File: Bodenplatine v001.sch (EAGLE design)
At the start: 104 parts, among them K1 RY612012, K2 RY612012, K3 RY612012, K4 RY612012, K5 RY612012, K6 RY612012, K7 RY612012, K8 RY612012, K9 RY612012, Q1 BC846, Q2 BC846, Q3 BC846, Q4 BC846, Q5 BC846, Q6 BC846, Q7 BC846, Q8 BC846, Q9 BC846, X1 SPRINGCON_AST125_5X2, X10 SPRINGCON_AST125_3X2, X11 SPRINGCON_AST125_4X2, X12 SPRINGCON_AST125_4X2, X13 SPRINGCON_AST125_5X2, X14 236-403, X15 236-402, X2 SPRINGCON_AST125_5X2, X3 SPRINGCON_AST125_5X2, X4 SPRINGCON_AST125_5X2, X5 SPRINGCON_AST125_5X2, X6 SPRINGCON_AST125_5X2, X7 SPRINGCON_AST125_5X2, X8 SPRINGCON_AST125_5X2, X9 SPRINGCON_AST125_5X2

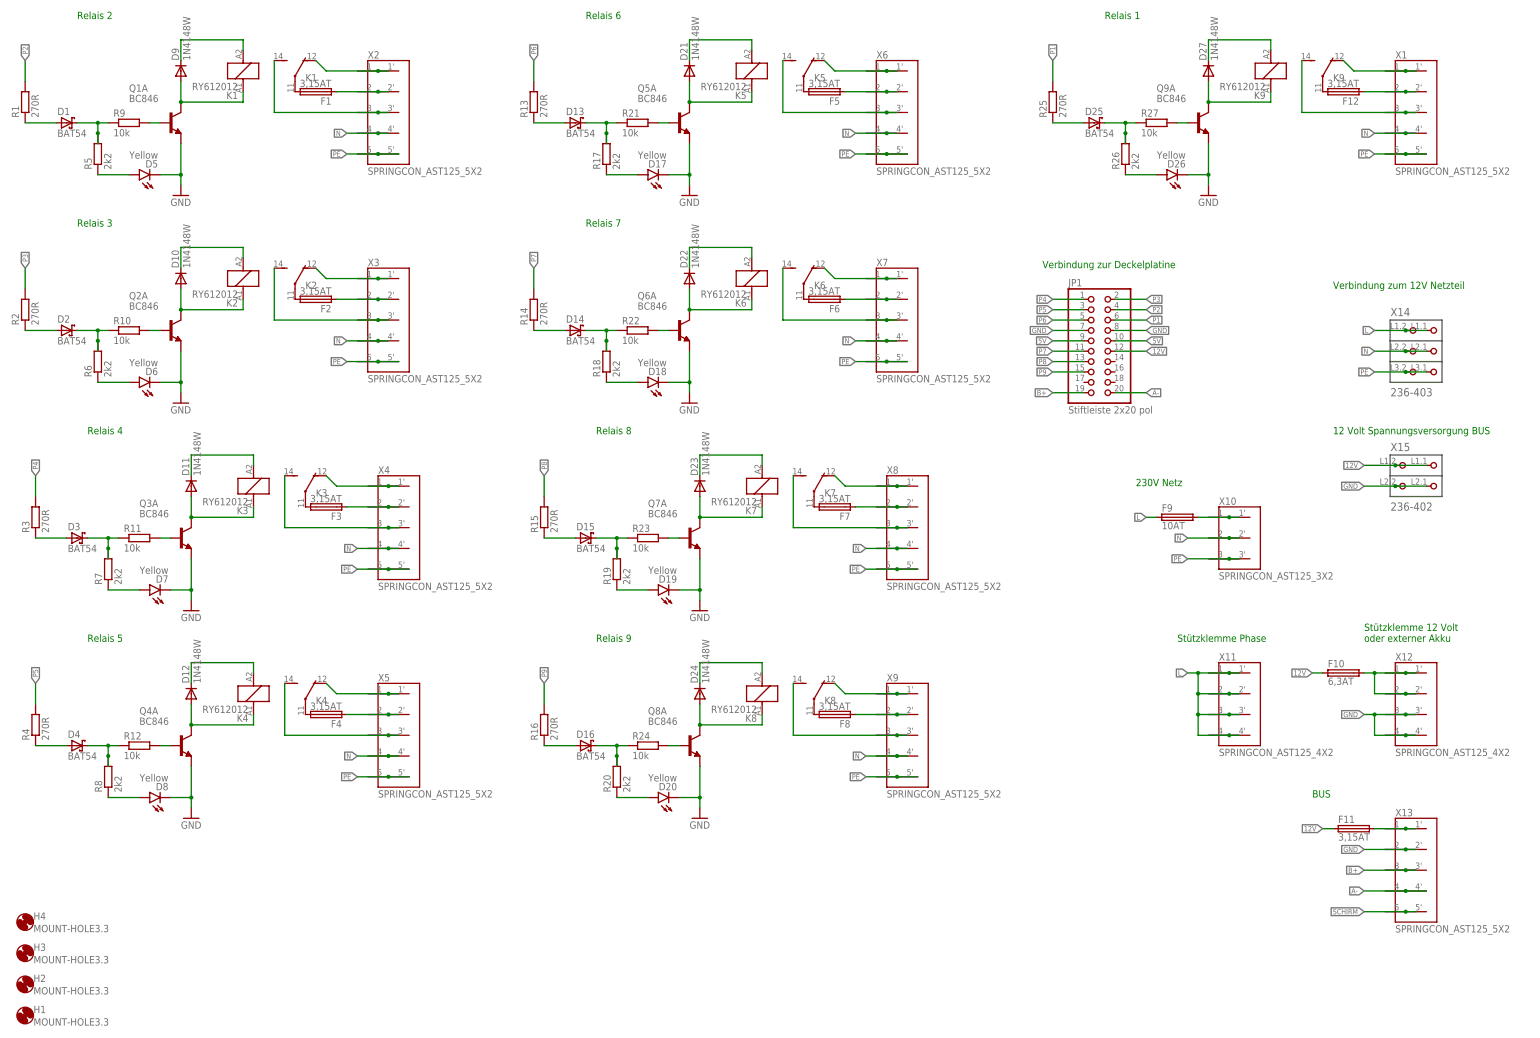
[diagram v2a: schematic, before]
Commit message: Relais neu sortiert (umbenannt)
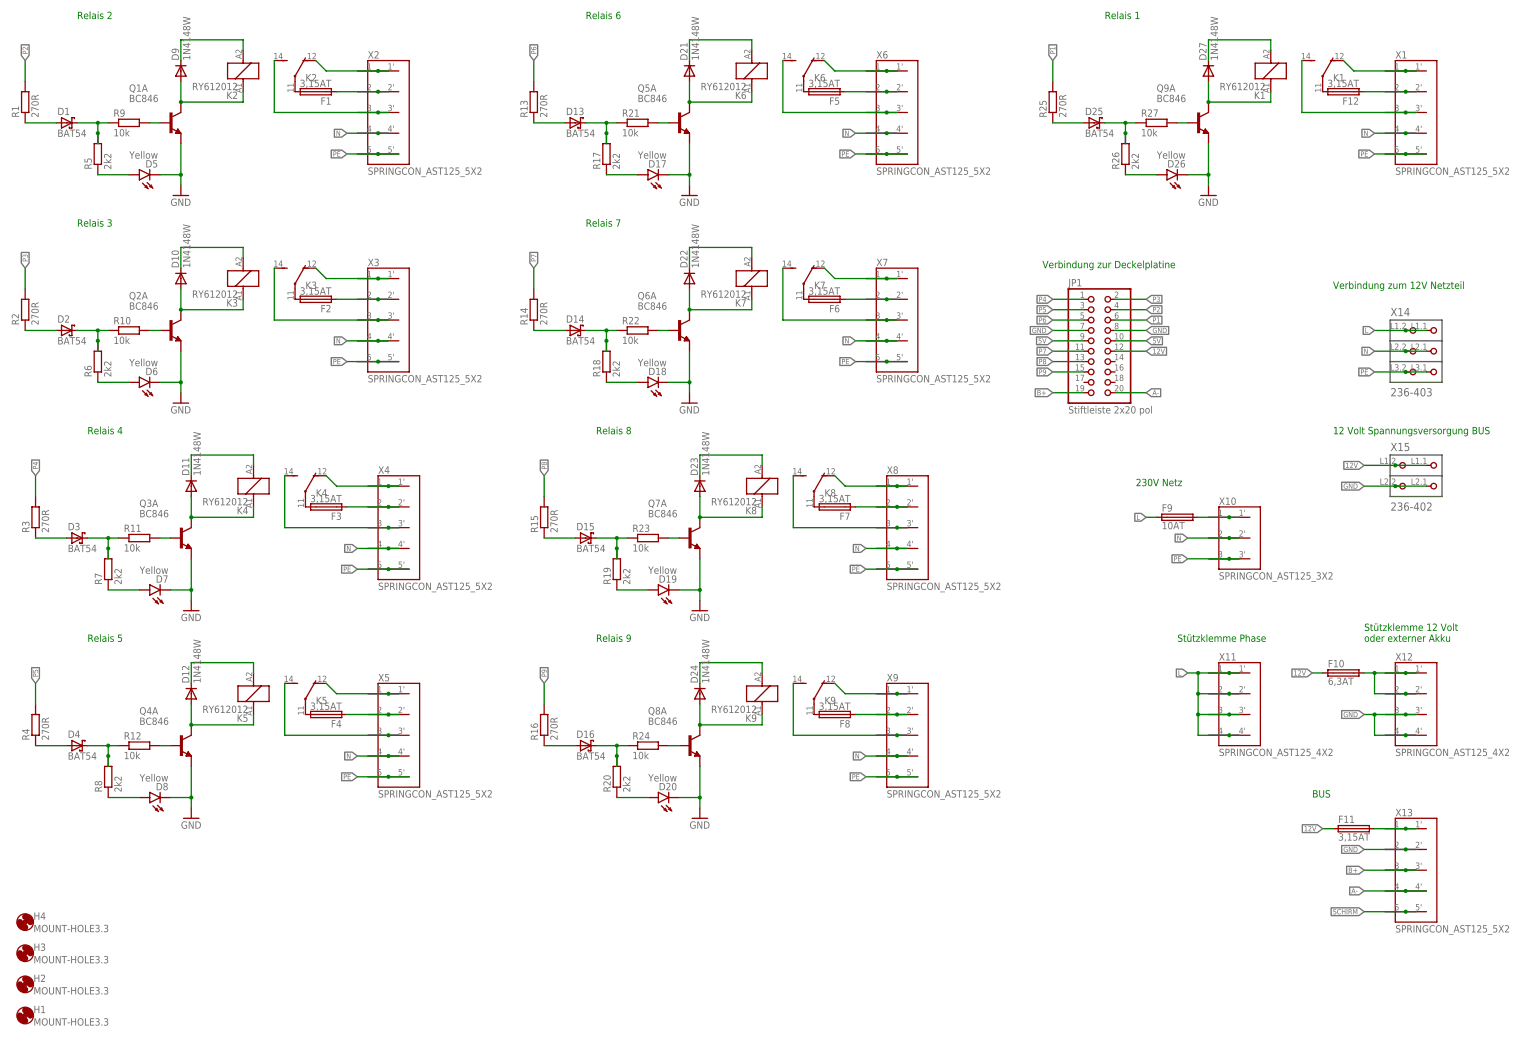
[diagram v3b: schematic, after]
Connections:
- net N$11: now also K21.2; no longer K11.2
- net N$12: now also K32.P; no longer K22.P
- net N$17: now also K31.2; no longer K21.2
- net N$18: now also K31.1; no longer K21.1
- net N$2: now also K22.S; no longer K12.S
- net N$20: now also K32.O; no longer K22.O
- net N$21: now also K42.S; no longer K32.S
- net N$22: now also K42.P; no longer K32.P
- net N$27: now also K41.2; no longer K31.2
- net N$28: now also K41.1; no longer K31.1
- net N$3: now also K22.P; no longer K12.P
- net N$30: now also K42.O; no longer K32.O
- net N$31: now also K52.S; no longer K42.S
- net N$32: now also K52.P; no longer K42.P
- net N$37: now also K51.2; no longer K41.2
- net N$38: now also K51.1; no longer K41.1
- net N$4: now also K22.O; no longer K12.O
- net N$40: now also K52.O; no longer K42.O
- net N$41: now also K62.S; no longer K52.S
- net N$42: now also K62.P; no longer K52.P
- net N$47: now also K61.2; no longer K51.2
- net N$48: now also K61.1; no longer K51.1
- net N$5: now also K21.1; no longer K11.1
- net N$50: now also K62.O; no longer K52.O
- net N$51: now also K72.S; no longer K62.S
- net N$52: now also K72.P; no longer K62.P
- net N$57: now also K71.2; no longer K61.2
- net N$58: now also K71.1; no longer K61.1
- net N$6: now also K32.S; no longer K22.S
- net N$60: now also K72.O; no longer K62.O
- net N$61: now also K82.S; no longer K72.S
- net N$62: now also K82.P; no longer K72.P
- net N$67: now also K81.2; no longer K71.2
- net N$68: now also K81.1; no longer K71.1
- net N$70: now also K82.O; no longer K72.O
- net N$71: now also K92.S; no longer K82.S
- net N$72: now also K92.P; no longer K82.P
- net N$77: now also K91.2; no longer K81.2
- net N$78: now also K91.1; no longer K81.1
- net N$80: now also K92.O; no longer K82.O
- net N$81: now also K12.S; no longer K92.S
- net N$82: now also K12.P; no longer K92.P
- net N$87: now also K11.2; no longer K91.2
- net N$88: now also K11.1; no longer K91.1
- net N$90: now also K12.O; no longer K92.O
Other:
- moved on the sheet: K1, K2, K3, K4, K5, K6, K7, K8, K9

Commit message: Tiny Switches über den Relais vergessen
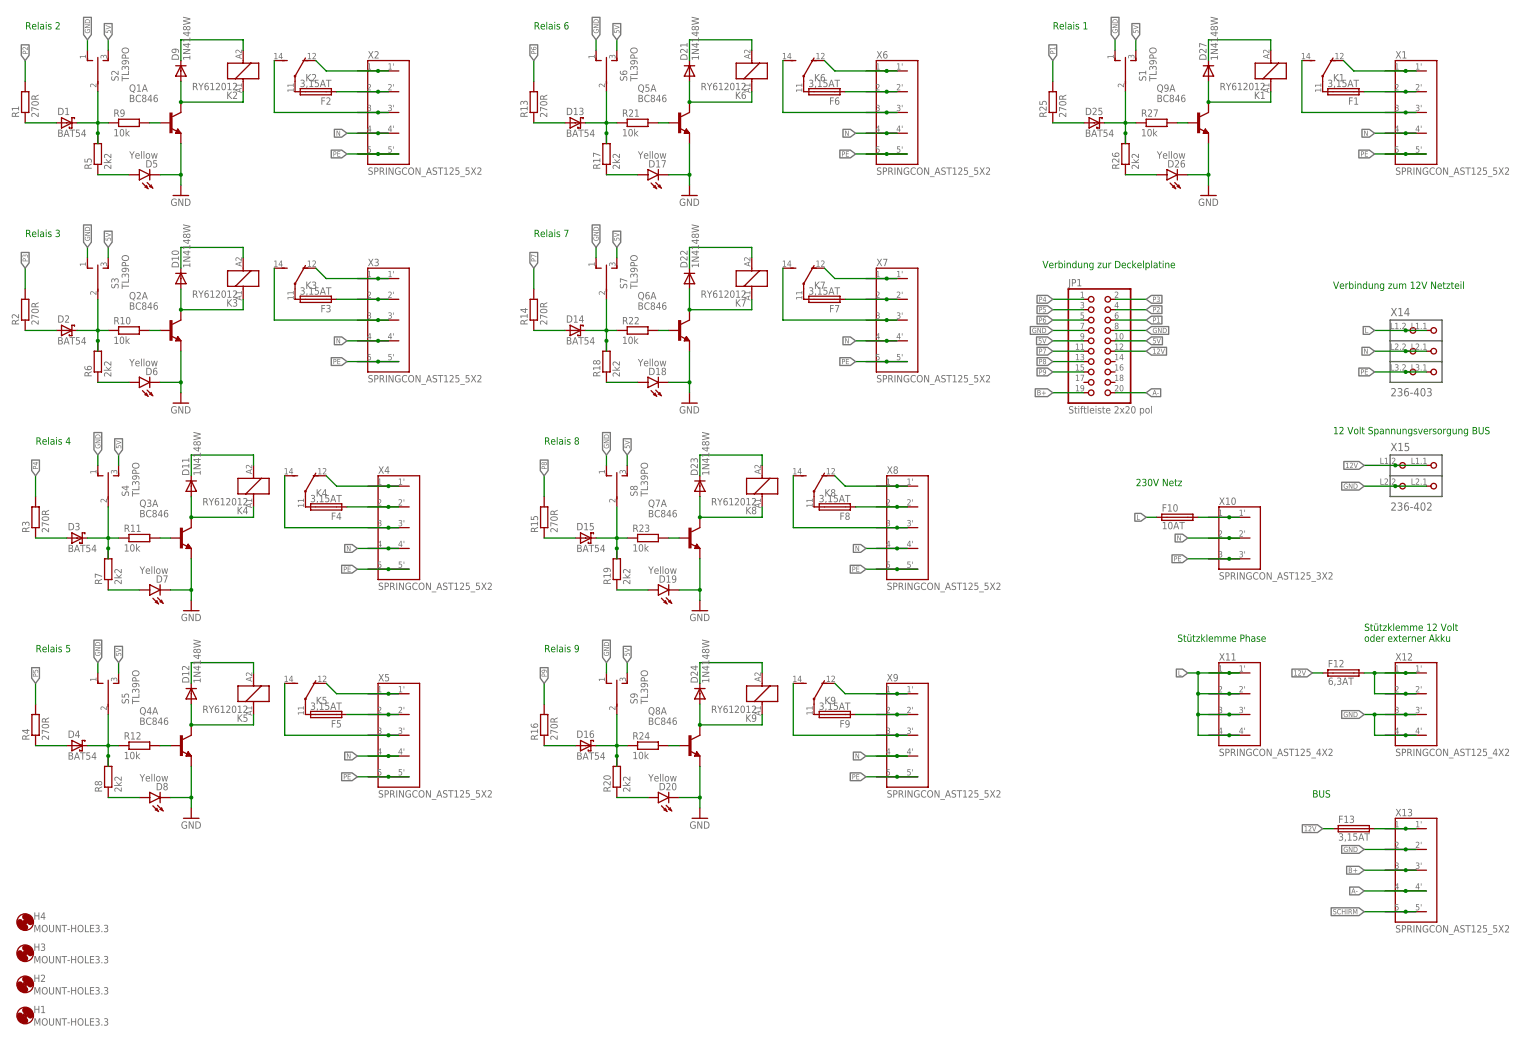
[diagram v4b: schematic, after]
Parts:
- added S1, S2, S3, S4, S5, S6, S7, S8, S9: TL39PO, xMZ-Mod-Touch-Bodenplatine:TL39PO
- F10: value 6,3AT -> 10AT
- F12: value 3,15AT -> 6,3AT
- F9: value 10AT -> 3,15AT
- renumbered F11 to F13
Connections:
- net 12V: now also F12.1; no longer F10.1
- net 5V: now also S1.S, S2.S, S3.S, S4.S, S5.S, S6.S, S7.S, S8.S, S9.S
- net GND: now also S1.O, S2.O, S3.O, S4.O, S5.O, S6.O, S7.O, S8.O, S9.O
- net L: now also F10.1; no longer F9.1
- net N$1: now also F2.1; no longer F1.1
- net N$12: now also F3.2; no longer F2.2
- net N$14: now also S3.P
- net N$19: now also F3.1; no longer F2.1
- net N$22: now also F4.2; no longer F3.2
- net N$24: now also S4.P
- net N$29: now also F4.1; no longer F3.1
- net N$3: now also F2.2; no longer F1.2
- net N$32: now also F5.2; no longer F4.2
- net N$34: now also S5.P
- net N$39: now also F5.1; no longer F4.1
- net N$42: now also F6.2; no longer F5.2
- net N$44: now also S6.P
- net N$49: now also F6.1; no longer F5.1
- net N$52: now also F7.2; no longer F6.2
- net N$54: now also S7.P
- net N$59: now also F7.1; no longer F6.1
- net N$62: now also F8.2; no longer F7.2
- net N$64: now also S8.P
- net N$69: now also F8.1; no longer F7.1
- net N$72: now also F9.2; no longer F8.2
- net N$74: now also S9.P
- net N$79: now also F9.1; no longer F8.1
- net N$8: now also S2.P
- net N$82: now also F1.2; no longer F12.2
- net N$84: now also S1.P
- net N$89: now also F1.1; no longer F12.1
- net N$91: now also F10.2; no longer F9.2
- net N$94: now also F12.2; no longer F10.2
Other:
- moved on the sheet: F1, F10, F12, F2, F3, F4, F5, F6, F7, F8, F9
